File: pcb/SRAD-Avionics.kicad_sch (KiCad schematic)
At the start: 16 parts, among them J1 Conn_01x02_Socket, SW1 SW_DIP_x01, U2 STM32H503RBTx

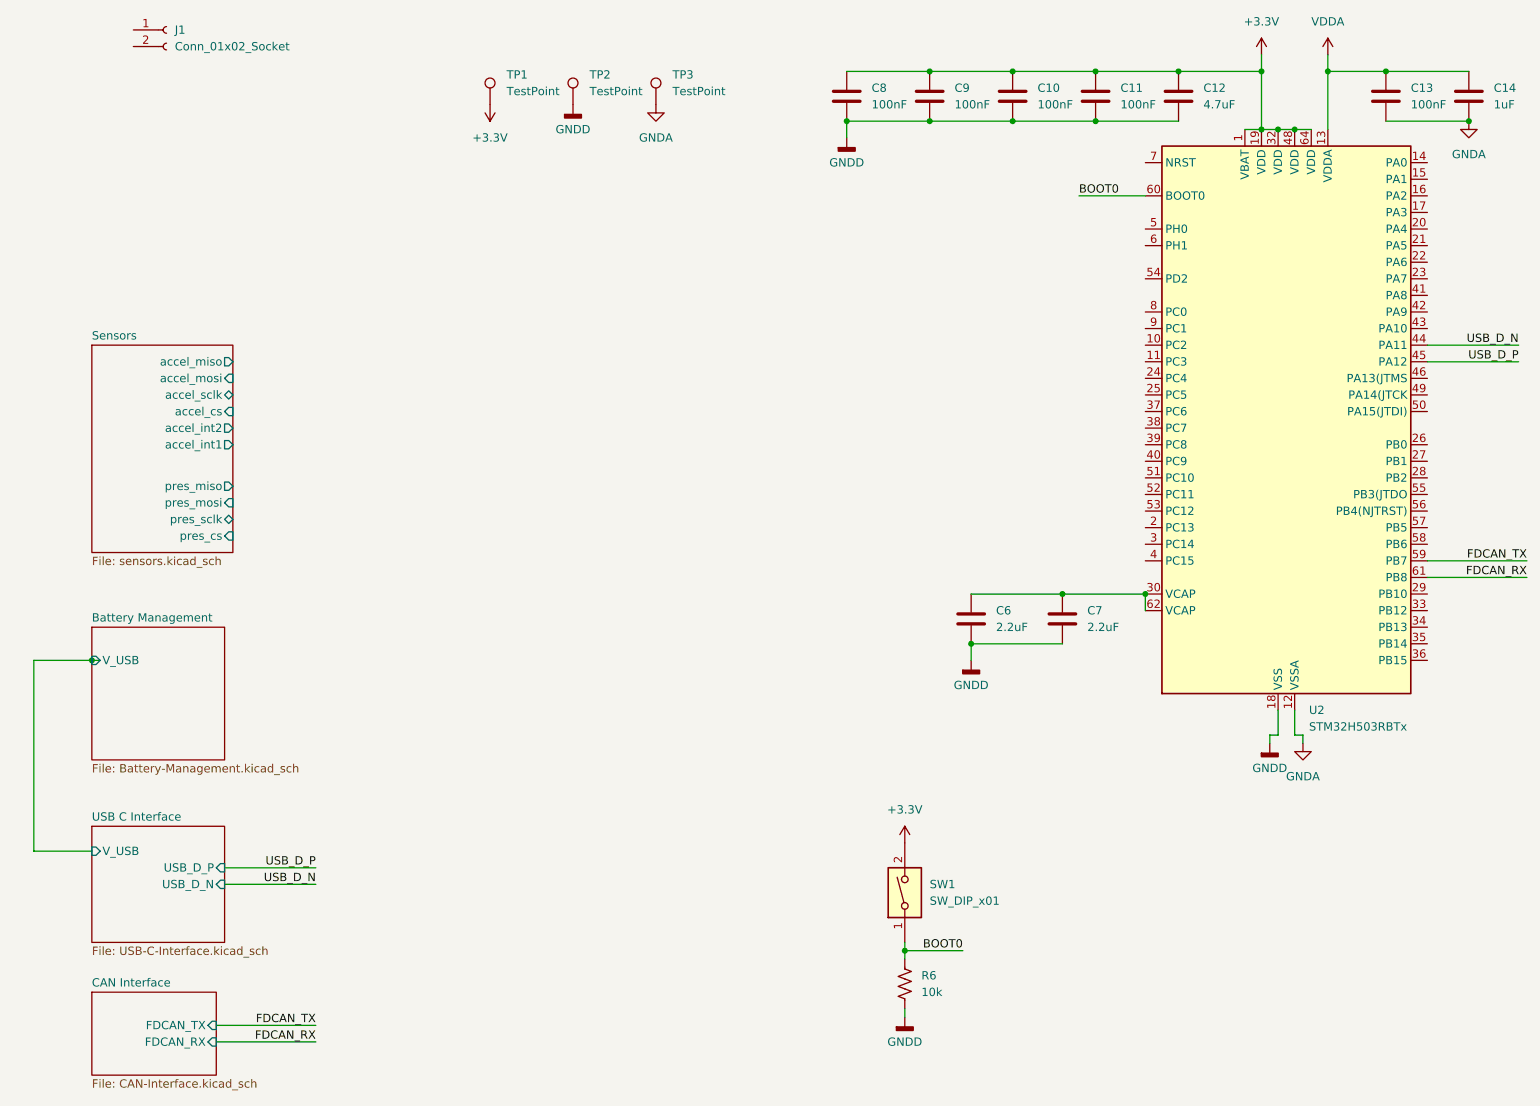
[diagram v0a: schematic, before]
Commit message: Routed reset monitor, all test points, 128 MBit flash, sensors, analog-digital jumper switches
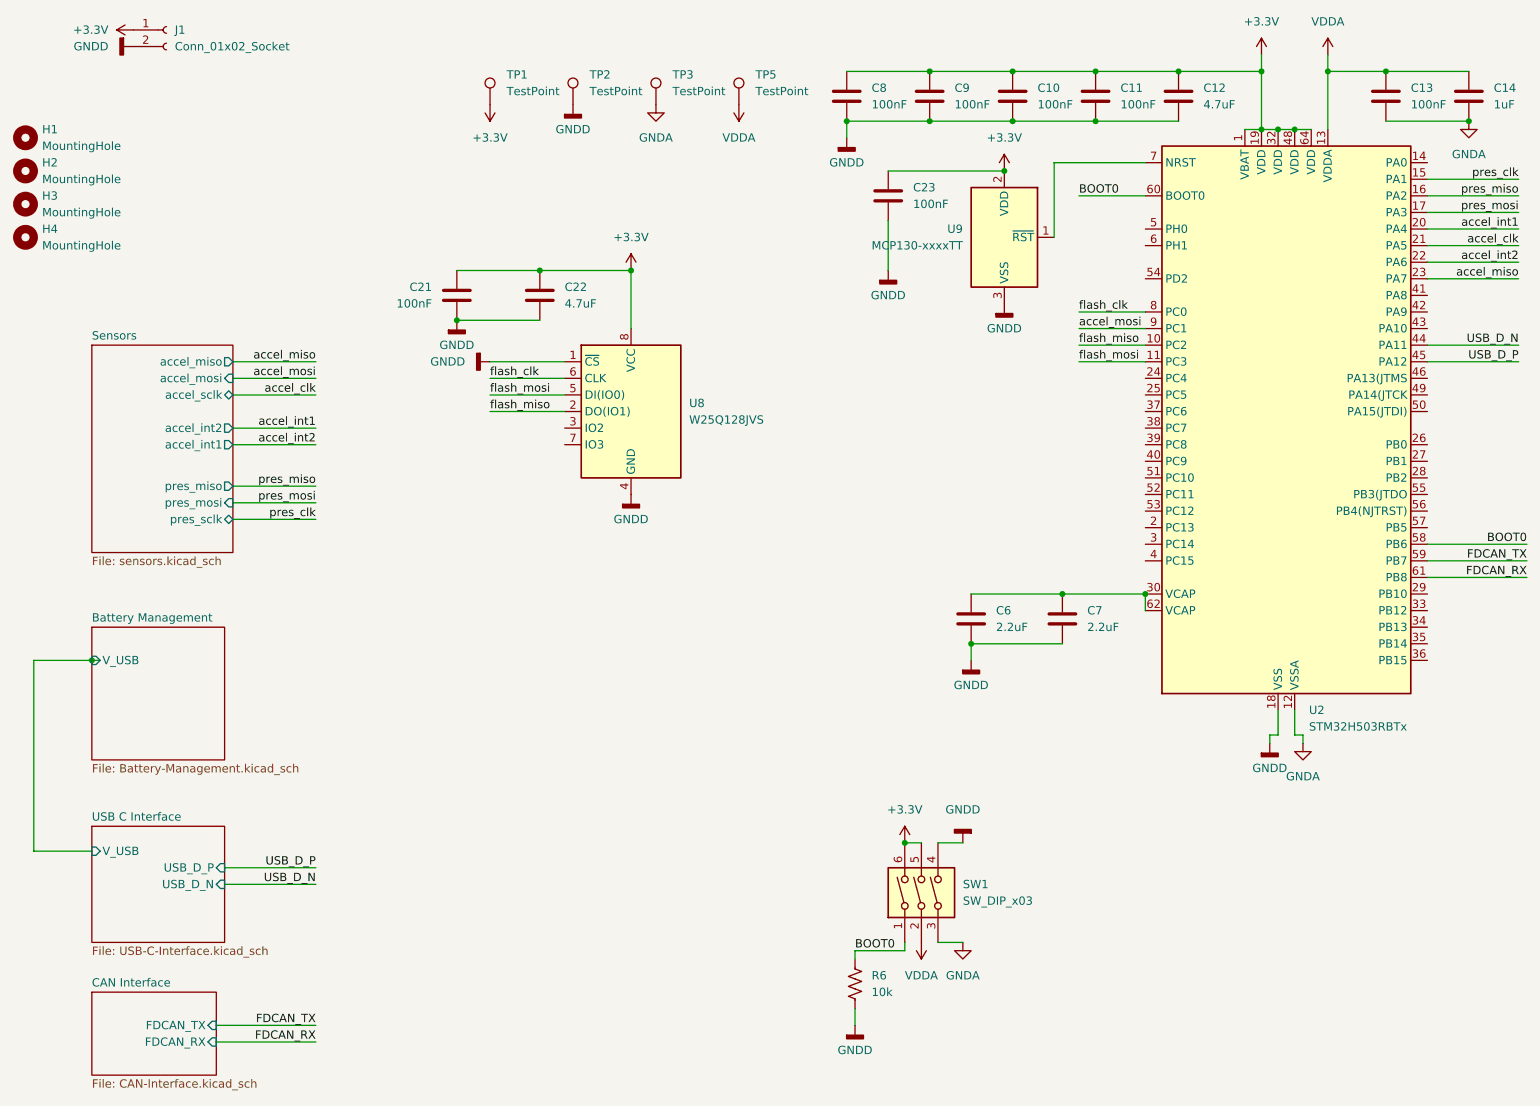
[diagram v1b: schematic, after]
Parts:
- removed SW1: SW_DIP_x01, Button_Switch_SMD:SW_DIP_SPSTx01_Slide_Copal_CHS-01B_W7.62mm_P1.27mm, symbol Switch:SW_DIP_x01
- added C21, C23: 100nF, Capacitor_SMD:C_0603_1608Metric_Pad1.08x0.95mm_HandSolder, symbol Device:C
- added C22: 4.7uF, Capacitor_SMD:C_0603_1608Metric_Pad1.08x0.95mm_HandSolder, symbol Device:C
- added H1, H2, H3, H4: MountingHole, MountingHole:MountingHole_3.2mm_M3, symbol Mechanical:MountingHole
- added SW1: SW_DIP_x03, Button_Switch_THT:SW_DIP_SPSTx03_Slide_9.78x9.8mm_W7.62mm_P2.54mm, symbol Switch:SW_DIP_x03
- added TP5: TestPoint, TestPoint:TestPoint_Loop_D2.60mm_Drill1.6mm_Beaded, symbol Connector:TestPoint
- added U8: W25Q128JVS, Package_SO:SOIC-8_5.23x5.23mm_P1.27mm, symbol Memory_Flash:W25Q128JVS
- added U9: MCP130-xxxxTT, Package_TO_SOT_SMD:SOT-23, symbol Power_Supervisor:MCP130-xxxxTT
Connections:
- net +3.3V: now also J1.1 (Pin_1), C21.1, C22.1, C23.1, SW1.5, SW1.6, U8.8 (VCC), U9.2 (VDD)
- net BOOT0: now also U2.58 (PB6), SW1.1
- net GNDA: now also SW1.3
- net GNDD: now also J1.2 (Pin_2), C21.2, C22.2, C23.2, SW1.4, U8.1 (~{CS}), U8.4 (GND), U9.3 (VSS)
- net VDDA: now also SW1.2, TP5.1
- net flash_miso: now reaches U2.10 (PC2)
- net flash_miso: now also U8.2 (DO(IO1))
- net flash_mosi: now reaches U2.11 (PC3)
- net flash_mosi: now also U8.5 (DI(IO0))
- net pres_clk: now reaches U2.15 (PA1)
- net pres_miso: now reaches U2.16 (PA2)
- net pres_mosi: now reaches U2.17 (PA3)
- net accel_int1: now reaches U2.20 (PA4)
- net accel_clk: now reaches U2.21 (PA5)
- net accel_int2: now reaches U2.22 (PA6)
- net accel_miso: now reaches U2.23 (PA7)
- net at U2.7 (NRST): now also U9.1 (~{RST})
- net flash_clk: now reaches U2.8 (PC0)
- net flash_clk: now also U8.6 (CLK)
- net accel_mosi: now reaches U2.9 (PC1)
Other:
- sheet Sensors ports: added none; removed accel_cs, pres_cs
- moved on the sheet: R6
